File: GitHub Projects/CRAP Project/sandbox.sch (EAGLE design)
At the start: 8 parts

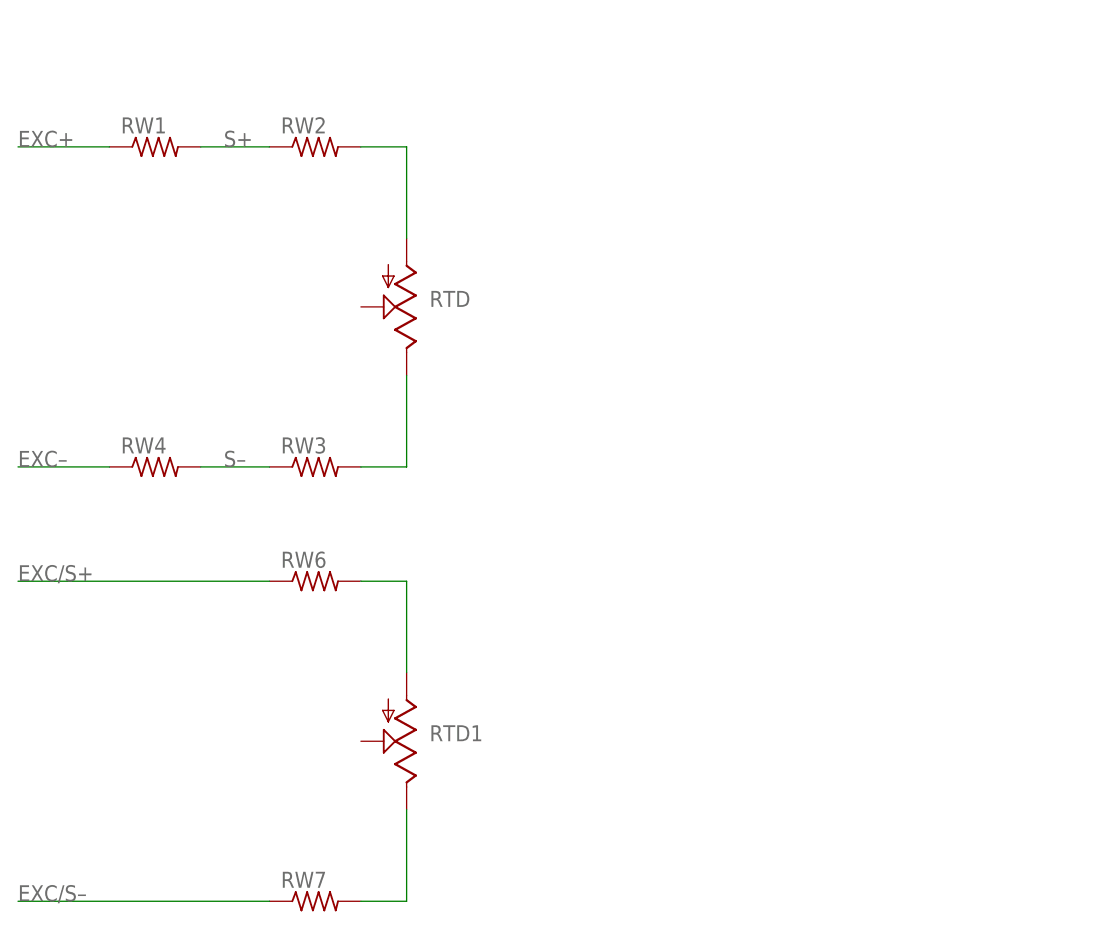
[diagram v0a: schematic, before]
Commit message: Added RTD module
Started the RTD module on Flight Computer schematic
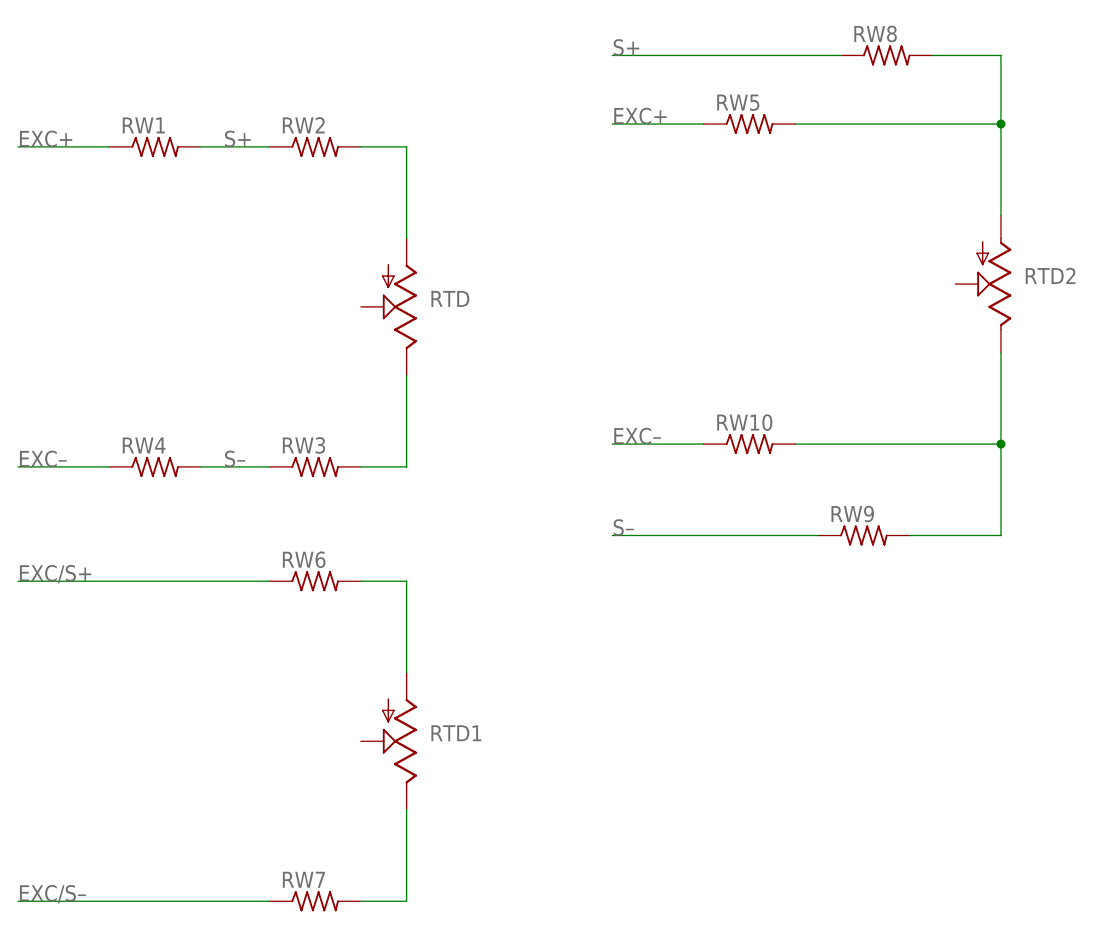
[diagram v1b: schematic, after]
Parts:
- added RTD2: (no value), pot:TRIM_US-3223G
- added RW10, RW5, RW8, RW9: (no value), rcl:R-US_R0603
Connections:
- new net N$5: RTD2.A, RW5.2, RW8.2
- new net N$6: RTD2.E, RW10.2, RW9.2
- net EXC+: now also RW5.1
- net EXC–: now also RW10.1
- net S+: now also RW8.1
- net S–: now also RW9.1
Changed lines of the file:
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@@
 <part name="RW6" library="rcl" deviceset="R-US_" device="R0603"/>
 <part name="RW7" library="rcl" deviceset="R-US_" device="R0603"/>
+<part name="RW5" library="rcl" deviceset="R-US_" device="R0603"/>
+<part name="RTD2" library="pot" deviceset="TRIM_US-" device="3223G"/>
+<part name="RW8" library="rcl" deviceset="R-US_" device="R0603"/>
+<part name="RW9" library="rcl" deviceset="R-US_" device="R0603"/>
+<part name="RW10" library="rcl" deviceset="R-US_" device="R0603"/>
 </parts>
 <sheets>
@@
 <attribute name="VALUE" x="69.85" y="-84.582" size="1.778" layer="96"/>
 </instance>
+<instance part="RW5" gate="G$1" x="121.92" y="5.08" smashed="yes">
+<attribute name="NAME" x="118.11" y="6.5786" size="1.778" layer="95"/>
+<attribute name="VALUE" x="118.11" y="1.778" size="1.778" layer="96"/>
+</instance>
+<instance part="RTD2" gate="G$1" x="149.86" y="-12.7" smashed="yes" rot="R180">
+<attribute name="NAME" x="152.4" y="-12.7" size="1.778" layer="95"/>
+<attribute name="VALUE" x="152.4" y="-10.16" size="1.778" layer="96" rot="R270"/>
+</instance>
+<instance part="RW8" gate="G$1" x="137.16" y="12.7" smashed="yes">
+<attribute name="NAME" x="133.35" y="14.1986" size="1.778" layer="95"/>
+<attribute name="VALUE" x="133.35" y="9.398" size="1.778" layer="96"/>
+</instance>
+<instance part="RW9" gate="G$1" x="134.62" y="-40.64" smashed="yes">
+<attribute name="NAME" x="130.81" y="-39.1414" size="1.778" layer="95"/>
+<attribute name="VALUE" x="130.81" y="-43.942" size="1.778" layer="96"/>
+</instance>
+<instance part="RW10" gate="G$1" x="121.92" y="-30.48" smashed="yes">
+<attribute name="NAME" x="118.11" y="-28.9814" size="1.778" layer="95"/>
+<attribute name="VALUE" x="118.11" y="-33.782" size="1.778" layer="96"/>
+</instance>
 </instances>
 <busses>
@@
 <label x="40.64" y="2.54" size="1.778" layer="95"/>
 </segment>
+<segment>
+<pinref part="RW5" gate="G$1" pin="1"/>
+<wire x1="106.68" y1="5.08" x2="116.84" y2="5.08" width="0.1524" layer="91"/>
+<label x="106.68" y="5.08" size="1.778" layer="95"/>
+</segment>
 </net>
 <net name="S+" class="0">
@@
 <wire x1="60.96" y1="2.54" x2="68.58" y2="2.54" width="0.1524" layer="91"/>
 <label x="63.5" y="2.54" size="1.778" layer="95"/>
+</segment>
+<segment>
+<pinref part="RW8" gate="G$1" pin="1"/>
+<wire x1="132.08" y1="12.7" x2="106.68" y2="12.7" width="0.1524" layer="91"/>
+<label x="106.68" y="12.7" size="1.778" layer="95"/>
 </segment>
 </net>
@@
 <label x="63.5" y="-33.02" size="1.778" layer="95"/>
 </segment>
+<segment>
+<pinref part="RW9" gate="G$1" pin="1"/>
+<wire x1="129.54" y1="-40.64" x2="106.68" y2="-40.64" width="0.1524" layer="91"/>
+<label x="106.68" y="-40.64" size="1.778" layer="95"/>
+</segment>
 </net>
 <net name="EXC–" class="0">
@@
 <wire x1="50.8" y1="-33.02" x2="40.64" y2="-33.02" width="0.1524" layer="91"/>
 <label x="40.64" y="-33.02" size="1.778" layer="95"/>
+</segment>
+<segment>
+<pinref part="RW10" gate="G$1" pin="1"/>
+<wire x1="116.84" y1="-30.48" x2="106.68" y2="-30.48" width="0.1524" layer="91"/>
+<label x="106.68" y="-30.48" size="1.778" layer="95"/>
 </segment>
 </net>
@@
 </segment>
 </net>
+<net name="N$5" class="0">
+<segment>
+<pinref part="RW5" gate="G$1" pin="2"/>
+<wire x1="127" y1="5.08" x2="149.86" y2="5.08" width="0.1524" layer="91"/>
+<pinref part="RTD2" gate="G$1" pin="A"/>
+<wire x1="149.86" y1="5.08" x2="149.86" y2="-5.08" width="0.1524" layer="91"/>
+<pinref part="RW8" gate="G$1" pin="2"/>
+<wire x1="142.24" y1="12.7" x2="149.86" y2="12.7" width="0.1524" layer="91"/>
+<wire x1="149.86" y1="12.7" x2="149.86" y2="5.08" width="0.1524" layer="91"/>
+<junction x="149.86" y="5.08"/>
+</segment>
+</net>
+<net name="N$6" class="0">
+<segment>
+<pinref part="RTD2" gate="G$1" pin="E"/>
+<wire x1="149.86" y1="-20.32" x2="149.86" y2="-30.48" width="0.1524" layer="91"/>
+<pinref part="RW10" gate="G$1" pin="2"/>
+<wire x1="149.86" y1="-30.48" x2="127" y2="-30.48" width="0.1524" layer="91"/>
+<pinref part="RW9" gate="G$1" pin="2"/>
+<wire x1="139.7" y1="-40.64" x2="149.86" y2="-40.64" width="0.1524" layer="91"/>
+<wire x1="149.86" y1="-40.64" x2="149.86" y2="-30.48" width="0.1524" layer="91"/>
+<junction x="149.86" y="-30.48"/>
+</segment>
+</net>
